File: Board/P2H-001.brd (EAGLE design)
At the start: 72 x 72 mm, 36 parts, among them IC1 4051N, IC2 LTC485N, IC3 74LS07N, IC4 LTC485N, K1 G5V-2, K2 G5V-2, T1 2SC1815, U1 ARDUINO_PRO_MINI, U2 MAX7219DIP

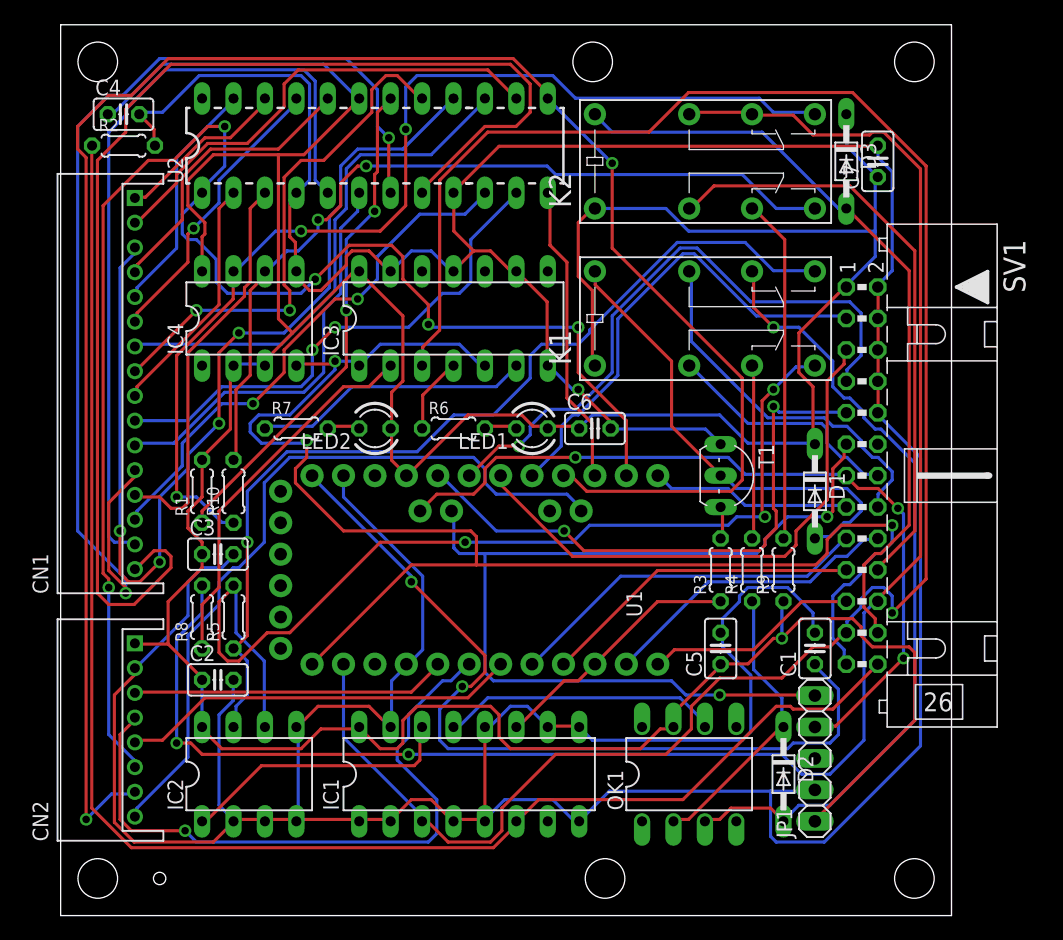
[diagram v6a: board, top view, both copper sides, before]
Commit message: Develop for R0.6
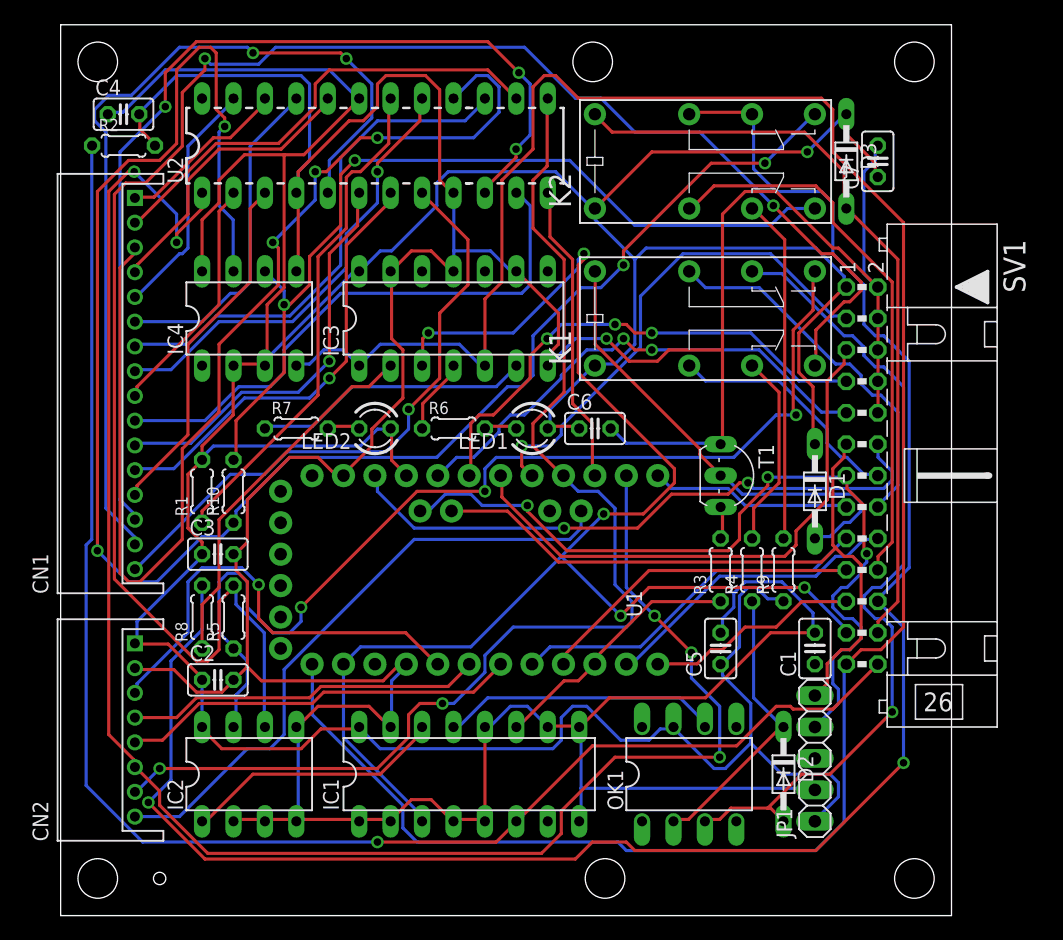
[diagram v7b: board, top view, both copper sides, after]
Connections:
- new net RST: SV1.12, U1.22
- net VDD: no longer U1.24
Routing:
- net VDD: track 68.5 -> 0.00 mm, vias 2 -> 0
- net RX+: track 82.5 -> 146.0 mm, vias 3 -> 2
- net COM1: track 121.1 -> 184.2 mm, vias 3 -> 0
- net SYS5: track 155.8 -> 96.8 mm
- net MIDI7: track 86.0 -> 143.6 mm, vias 3 -> 4
- net LD7: track 101.1 -> 49.4 mm, vias 0 -> 1
- net LD3: track 87.0 -> 35.8 mm, vias 2 -> 1
- net RST: track 0.00 -> 49.6 mm, vias 0 -> 2
- net COM0: track 164.8 -> 116.3 mm, vias 1 -> 5
- net LD5: track 42.9 -> 80.4 mm, vias 2 -> 3
- net GND: track 390.6 -> 364.0 mm
- net SYS1: track 53.3 -> 28.9 mm, vias 1 -> 0
- net IOC8: track 78.6 -> 57.3 mm, vias 2 -> 0
- net SYS3: track 124.0 -> 143.1 mm
- net MIDI3: track 140.3 -> 153.4 mm
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
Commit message: Now ready for R0.6.
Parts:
- added JP2: (no value), pinhead:1X01
- CN2: device jst-ph:S8B-PH-K-S -> jst-ph:S10B-PH-K-S
- R5: value 120 -> 330
- R7: value 330 -> 120
- moved C4 65.5 mm to (43.2, 11.4), turned to 90 degrees
- moved R2 60.7 mm to (53.3, 25.4)
- moved R5 42.7 mm to (53.3, 40.6), turned to 0 degrees
- moved R1 42.4 mm to (53.3, 27.9), turned to 0 degrees
- moved C5 41.4 mm to (40.6, 61.0)
- moved C6 35.3 mm to (61.0, 8.89), turned to 90 degrees
- moved LED2 34.5 mm to (59.7, 35.6)
- moved C3 32.7 mm to (20.3, 61.0), turned to 90 degrees
- moved R3 29.0 mm to (35.6, 50.8)
- moved T1 27.5 mm to (30.5, 50.8)
- moved D1 27.0 mm to (40.6, 52.1)
- moved R8 26.7 mm to (12.7, 50.8)
- moved R6 21.9 mm to (53.3, 35.6)
- moved LED1 21.6 mm to (59.7, 40.6)
- moved U2 20.4 mm to (24.1, 41.9)
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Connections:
- net IOC4 renamed GEEK0
- net IOC5 renamed GEEK1
- net IOC6 renamed GEEK2
- net IOC7 renamed GEEK3
- net IOC8 renamed GEEK4
- net IOC9 renamed GEEK5
- net LD0 renamed LDIG0
- net LD1 renamed LDIG1
- net LD2 renamed LDIG2
- net LD3 renamed LDIG3
- net LD4 renamed LDIG4
- net LD5 renamed LDIG5
- net LD6 renamed LDIG6
- net LD7 renamed LDIG7
- net LS0 renamed LSEG0
- net LS1 renamed LSEG1
- net LS2 renamed LSEG2
- net LS3 renamed LSEG3
- net LS4 renamed LSEG4
- net LS5 renamed LSEG5
- net LS6 renamed LSEG6
- net LS7 renamed LSEG7
- net N$8 renamed TX+
- net N$9 renamed TXSRC
- net SYS0 renamed CTRL2
- net SYS1 renamed CTRL3
- net SYS2 renamed CTRL4
- net SYS3 renamed CTRL5
- removed net COM0: IC1.3, IC3.3, SV1.23, U1.2
- removed net COM1: IC3.1, IC3.5, IC4.4, SV1.25, U1.1
- removed net COM3: SV1.18, U1.11
- removed net IOC0: SV1.17, U1.8
- removed net IOC1: SV1.19, U1.9
- removed net IOC2: SV1.21, U1.12
- removed net IOC3: SV1.15, U1.13
- removed net RST: SV1.12, U1.22
- removed net SYS4: U1.15, U2.12
- removed net SYS5: CN2.7, U1.16, U2.13
- removed net SYS6: CN2.8, U1.A6
- removed net SYS7: U1.A7
- removed net VDD: C1.1
- new net ANLG0: CN2.9, U1.A6
- new net ANLG1: CN2.10, U1.A7
- new net CTRL0: JP2.1, SV1.23
- new net CTRL1: IC1.6, R2.1, SV1.25
- new net CTRL6: CN2.7, U1.15, U2.12
- new net CTRL7: CN2.8, U1.16, U2.13
- new net CTRL8: U1.10
- new net CTRL9: U1.3
- new net GEEK6: SV1.15, U1.8
- new net GEEK7: SV1.17, U1.9
- new net GEEK8: SV1.19, U1.12
- new net GEEK9: SV1.21, U1.13
- new net MIDI6: K2.13, SV1.24
- new net N$25: IC3.1, IC4.4
- new net TX-: IC4.7, K2.9, R10.1, SV1.26
- new net TXSNK: K2.11, R8.2
- net COM2: no longer U1.10
- net GND: no longer U1.4
- net MIDI0: now also IC1.3, IC3.3, SV1.12, U1.2; no longer K1.4, SV1.14
- net MIDI1: now also IC3.5, SV1.14, U1.1; no longer K1.13, SV1.16
- net MIDI2: now also K1.4, SV1.16; no longer K2.4, SV1.20
- net MIDI3: now also K1.13, SV1.18; no longer K2.11, K2.13, R8.2, SV1.22
- net MIDI4: now also SV1.20, U1.11; no longer D3.A, K2.16, SV1.24
- net MIDI5: now also K2.4, SV1.22; no longer IC1.6, R2.1, SV1.26
- net MIDI7: now also D3.A, K2.16; no longer IC4.7, K2.9, R10.1
- net N$3: now also R5.1; no longer R6.1
- net N$4: now also R6.1; no longer R7.1
- net N$5: now also R5.2; no longer R6.2
- net N$6: now also R6.2; no longer R7.2
- net RX+: now also R7.2; no longer R5.2
- net RX-: now also R7.1; no longer R5.1
- net VCC: now also C1.1
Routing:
- net COM1: track 184.2 -> 0.00 mm
- net CTRL6: track 0.00 -> 181.6 mm, vias 0 -> 3
- net TX-: track 0.00 -> 141.9 mm, vias 0 -> 6
- net MIDI0: track 19.6 -> 158.6 mm, vias 0 -> 4
- net MIDI7: track 143.6 -> 23.5 mm, vias 4 -> 0
- net COM0: track 116.3 -> 0.00 mm, vias 5 -> 0
- net MIDI1: track 30.3 -> 145.2 mm, vias 0 -> 2
- net MIDI3: track 153.4 -> 43.6 mm, vias 2 -> 0
- net CTRL0: track 0.00 -> 106.3 mm, vias 0 -> 2
- net SYS5: track 96.8 -> 0.00 mm, vias 2 -> 0
- net CTRL2: track 36.3 -> 128.0 mm, vias 1 -> 2
- net CTRL5: track 143.1 -> 67.2 mm, vias 5 -> 2
- net CTRL7: track 0.00 -> 68.0 mm, vias 0 -> 2
- net LSEG2: track 91.9 -> 30.9 mm, vias 3 -> 0
- net MIDI5: track 123.9 -> 63.0 mm, vias 1 -> 2
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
